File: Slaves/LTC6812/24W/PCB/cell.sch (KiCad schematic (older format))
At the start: 7 parts, among them Q2 TSM2323

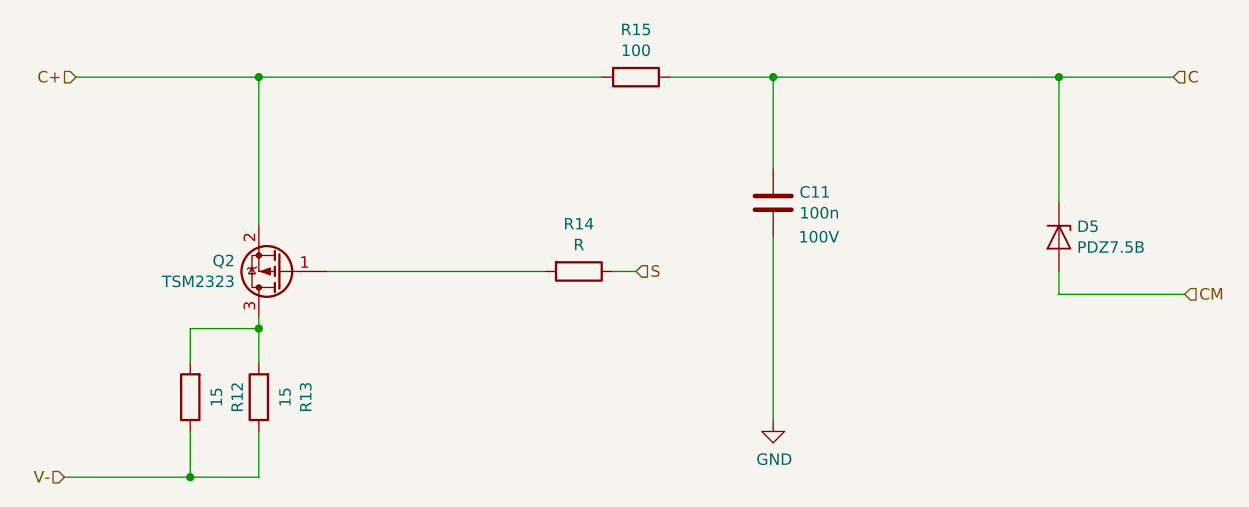
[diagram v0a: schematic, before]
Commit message: LTC6812 12W & 24W versions
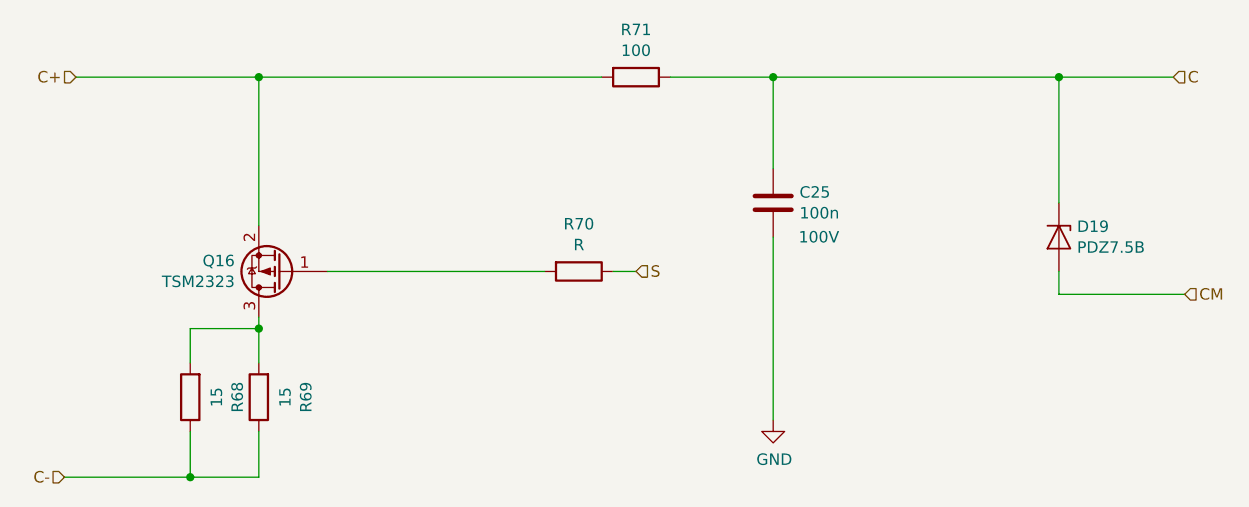
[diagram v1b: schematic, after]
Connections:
- net V- renamed C-
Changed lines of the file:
@@
 EESchema Schematic File Version 5
-LIBS:LTC6813-cache
+LIBS:LTC6812-cache
 EELAYER 30 0
 EELAYER END
 $Descr A4 11693 8268
 encoding utf-8
-Sheet 2 19
+Sheet 16 16
 Title ""
 Date ""
@@
 AR Path="/5B510167/5B4FCD15" Ref="C27"  Part="1"
 AR Path="/5B5115CC/5B4FCD15" Ref="C28"  Part="1"
-F 0 "C11" H 5535 3754 50  0000 R CNN
+F 0 "C25" H 5535 3754 50  0000 R CNN
 F 1 "100n" H 5535 3845 50  0000 R CNN
 F 2 "Capacitors_SMD:C_0603_HandSoldering" H 5688 3650 50  0001 C CNN
@@
 	4950 4100 5050 4100
 Text HLabel 2550 5000 0    50   Input ~ 0
-V-
+C-
 Text HLabel 7400 3250 2    50   Input ~ 0
 C
@@
 AR Path="/5B510167/5C6D9E32" Ref="R77"  Part="1"
 AR Path="/5B5115CC/5C6D9E32" Ref="R81"  Part="1"
-F 0 "R13" V 3193 4650 50  0000 C CNN
+F 0 "R69" V 3193 4650 50  0000 C CNN
 F 1 "15" V 3284 4650 50  0000 C CNN
 F 2 "Resistors_SMD:R_2512" V 3330 4650 50  0001 C CNN
@@
 AR Path="/5B510167/5C51375B" Ref="Q18"  Part="1"
 AR Path="/5B5115CC/5C51375B" Ref="Q19"  Part="1"
-F 0 "Q2" H 3705 4054 50  0000 L CNN
+F 0 "Q16" H 3705 4054 50  0000 L CNN
 F 1 "TSM2323" H 3705 4145 50  0000 L CNN
 F 2 "TO_SOT_Packages_SMD:SOT-23" H 3700 4200 50  0001 C CNN
@@
 AR Path="/5B510167/5D68BDCB" Ref="R76"  Part="1"
 AR Path="/5B5115CC/5D68BDCB" Ref="R80"  Part="1"
-F 0 "R12" V 2893 4650 50  0000 C CNN
+F 0 "R68" V 2893 4650 50  0000 C CNN
 F 1 "15" V 2984 4650 50  0000 C CNN
 F 2 "Resistors_SMD:R_2512" V 3030 4650 50  0001 C CNN
@@
 AR Path="/5B510167/5D68CA39" Ref="D21"  Part="1"
 AR Path="/5B5115CC/5D68CA39" Ref="D22"  Part="1"
-F 0 "D5" V 6854 4029 50  0000 L CNN
+F 0 "D19" V 6854 4029 50  0000 L CNN
 F 1 "PDZ7.5B" V 6945 4029 50  0000 L CNN
 F 2 "Diode_SMD:D_SOD-323_HandSoldering" H 6900 3950 50  0001 C CNN
@@
 AR Path="/5B510167/5D6BA91D" Ref="#PWR038"  Part="1"
 AR Path="/5B5115CC/5D6BA91D" Ref="#PWR039"  Part="1"
-F 0 "#PWR022" H 5650 4500 50  0001 C CNN
+F 0 "#PWR036" H 5650 4500 50  0001 C CNN
 F 1 "GND" H 5655 4577 50  0000 C CNN
 F 2 "" H 5650 4750 50  0001 C CNN
@@
 AR Path="/5B510167/5B4FCD0D" Ref="R79"  Part="1"
 AR Path="/5B5115CC/5B4FCD0D" Ref="R83"  Part="1"
-F 0 "R15" V 4843 3250 50  0000 C CNN
+F 0 "R71" V 4843 3250 50  0000 C CNN
 F 1 "100" V 4934 3250 50  0000 C CNN
 F 2 "Resistors_SMD:R_0603_HandSoldering" V 4980 3250 50  0001 C CNN
@@
 AR Path="/5B510167/5B4FCD21" Ref="R78"  Part="1"
 AR Path="/5B5115CC/5B4FCD21" Ref="R82"  Part="1"
-F 0 "R14" V 4593 4100 50  0000 C CNN
+F 0 "R70" V 4593 4100 50  0000 C CNN
 F 1 "R" V 4684 4100 50  0000 C CNN
 F 2 "Resistors_SMD:R_0603_HandSoldering" V 4730 4100 50  0001 C CNN
